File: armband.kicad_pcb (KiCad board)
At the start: 6 copper layers, 48.8 x 40.1 mm, 86 parts, among them IC1 QSMP-1570, IC10 TLE493DW2B6A0HTSA1, IC2 BMI323, IC3 TPS259571DSGR, IC4 TPD6E001RSERG4, IC5 MP2722GRH-0000-Z, IC6 TPS62291DRVR, IC7 TPS62293DRVR, IC8 BQ27427YZFR, IC9 nRF52832-CIAA-G-R7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

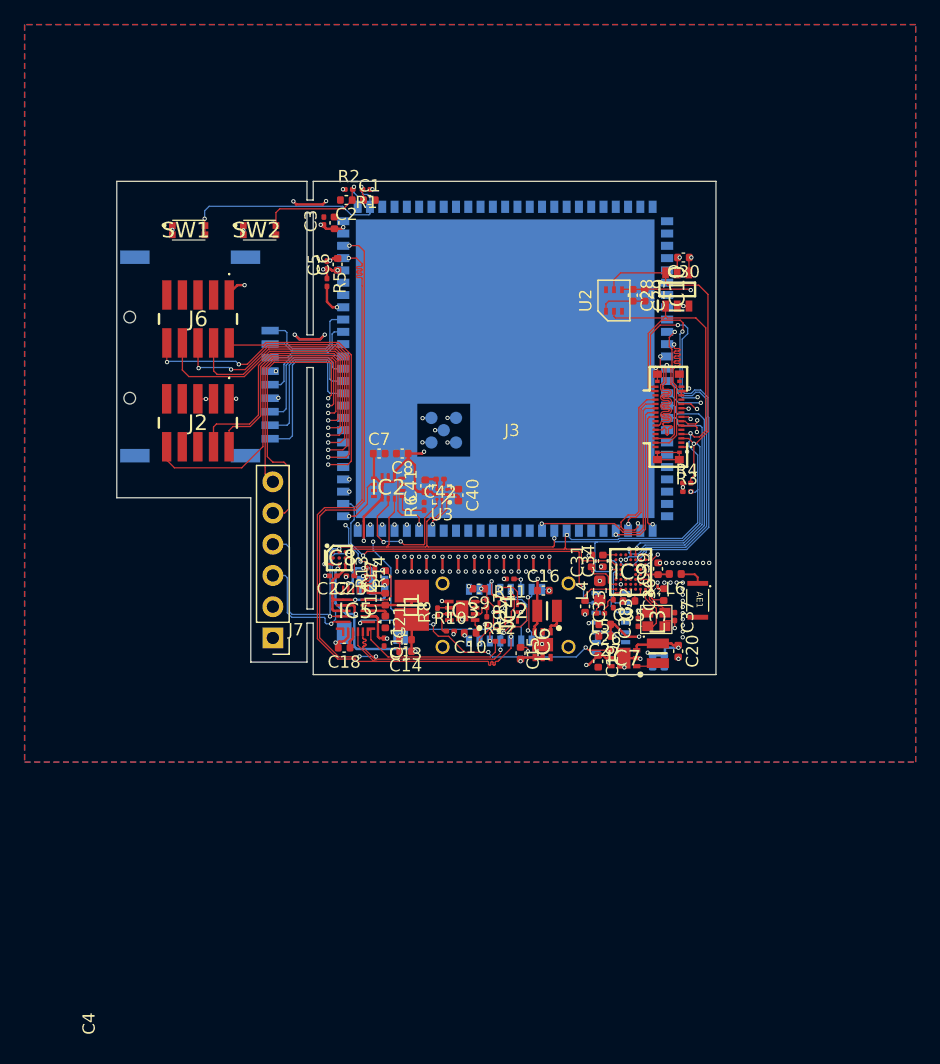
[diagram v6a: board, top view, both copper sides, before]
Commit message: added QSMP1570_better.kicad_mod and part designators, moved production files into own folder
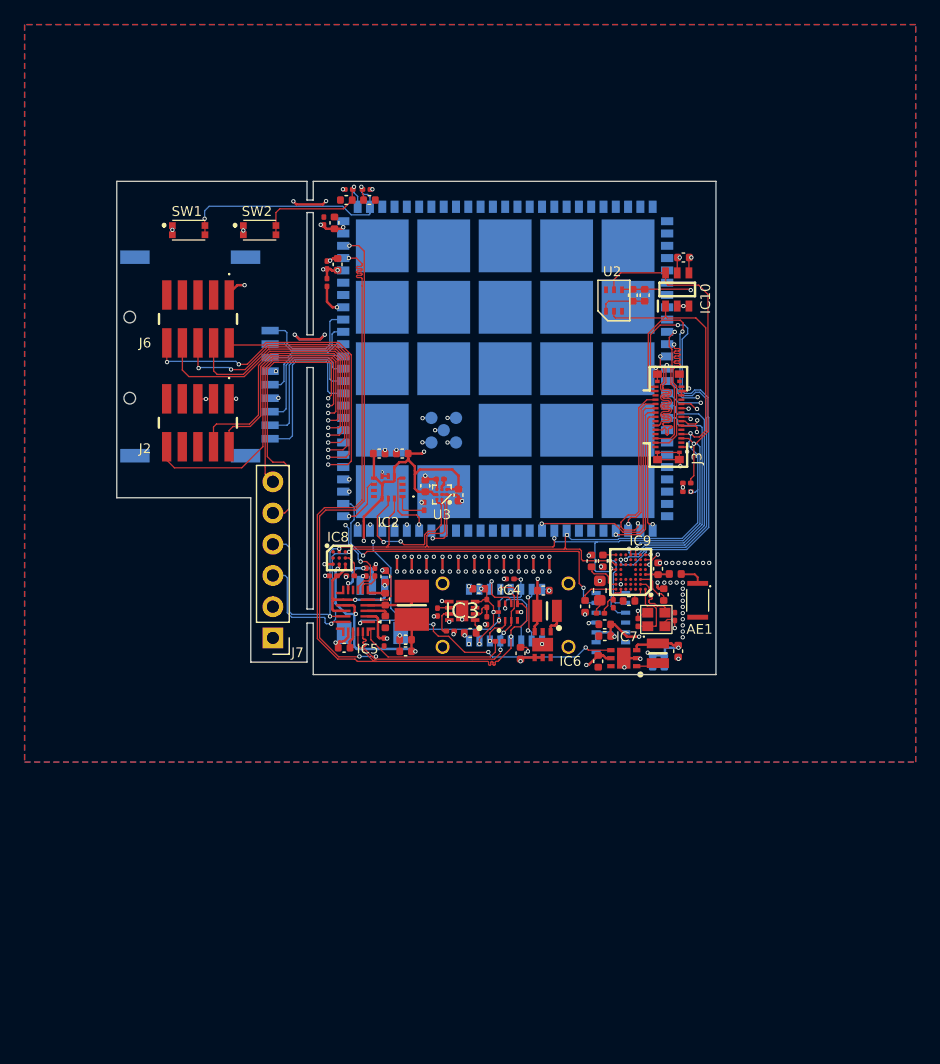
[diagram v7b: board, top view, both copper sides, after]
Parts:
- IC1: footprint ARMband:QSMP1570 -> ARMband:QSMP1570_better
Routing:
- net +1V8: track 84.2 -> 89.6 mm
- net GND: track 37.5 -> 39.9 mm, vias 78 -> 84
- net BMM350_INT: track 3.19 -> 4.84 mm
- net QSMP_SCL: track 101.2 -> 101.9 mm
- net Net-(IC9-XC1): track 3.60 -> 4.29 mm
- net QSMP_SDA: track 100.8 -> 101.4 mm

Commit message: Fix unconnected nets
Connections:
- U1 pad 1: Net-(U1-NC-Pad1) -> unconnected-(U1-NC-Pad1)
- U1 pad 14: Net-(U1-NC-Pad1) -> unconnected-(U1-NC-Pad14)
- U1 pad 5: Net-(U1-NC-Pad1) -> unconnected-(U1-NC-Pad5)
- U1 pad 6: Net-(U1-NC-Pad1) -> unconnected-(U1-NC-Pad6)
- U1 pad 7: Net-(U1-NC-Pad1) -> unconnected-(U1-NC-Pad7)
- U1 pad 8: Net-(U1-NC-Pad1) -> unconnected-(U1-NC-Pad8)
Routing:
- net GND: track 39.9 -> 50.8 mm, vias 84 -> 97
- net Net-(IC9-VDD_1): track 4.14 -> 9.96 mm, vias 0 -> 2
- net Net-(IC9-XC1): track 4.29 -> 5.09 mm
- net QSMP_SCL: track 101.9 -> 101.1 mm
- net QSMP_SDA: track 101.4 -> 100.7 mm
